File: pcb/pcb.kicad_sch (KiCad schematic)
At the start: 41 parts, among them J1 NMJ4HCD2, J2 NMJ4HCD2, J3 694106301002, SW1 FSWITCH, U1 RC4558, U2 L78L09_TO92

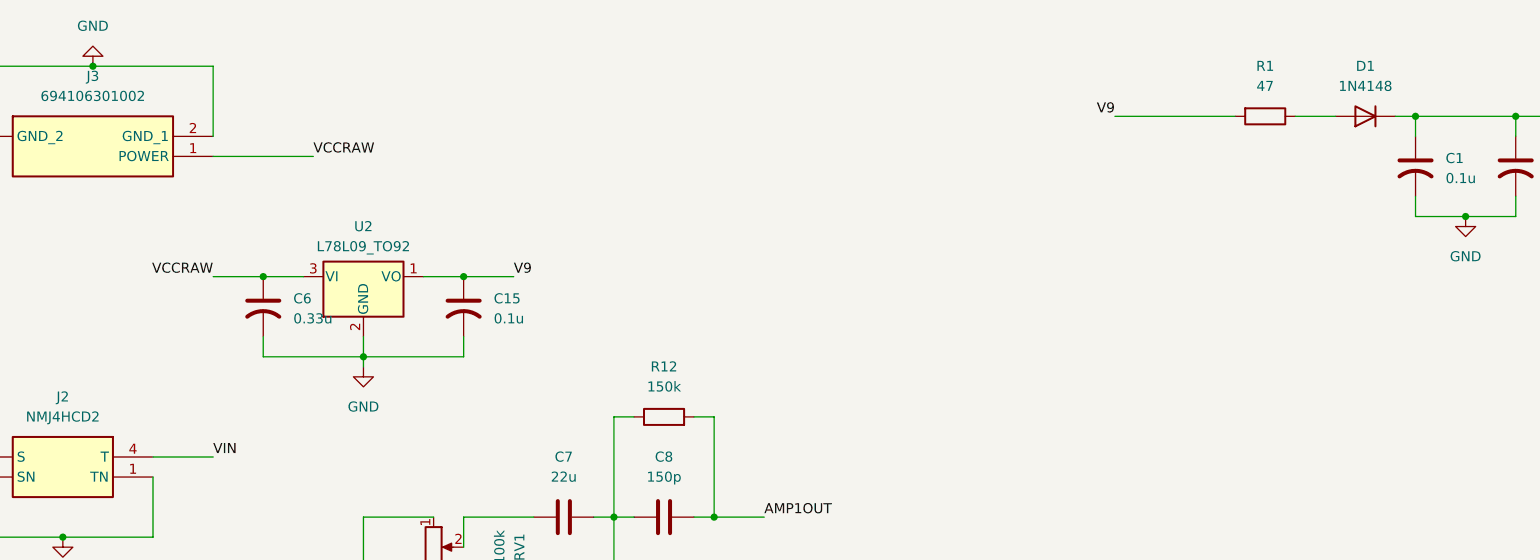
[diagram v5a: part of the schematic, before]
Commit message: Fix reverse polarity protection diode - schematic
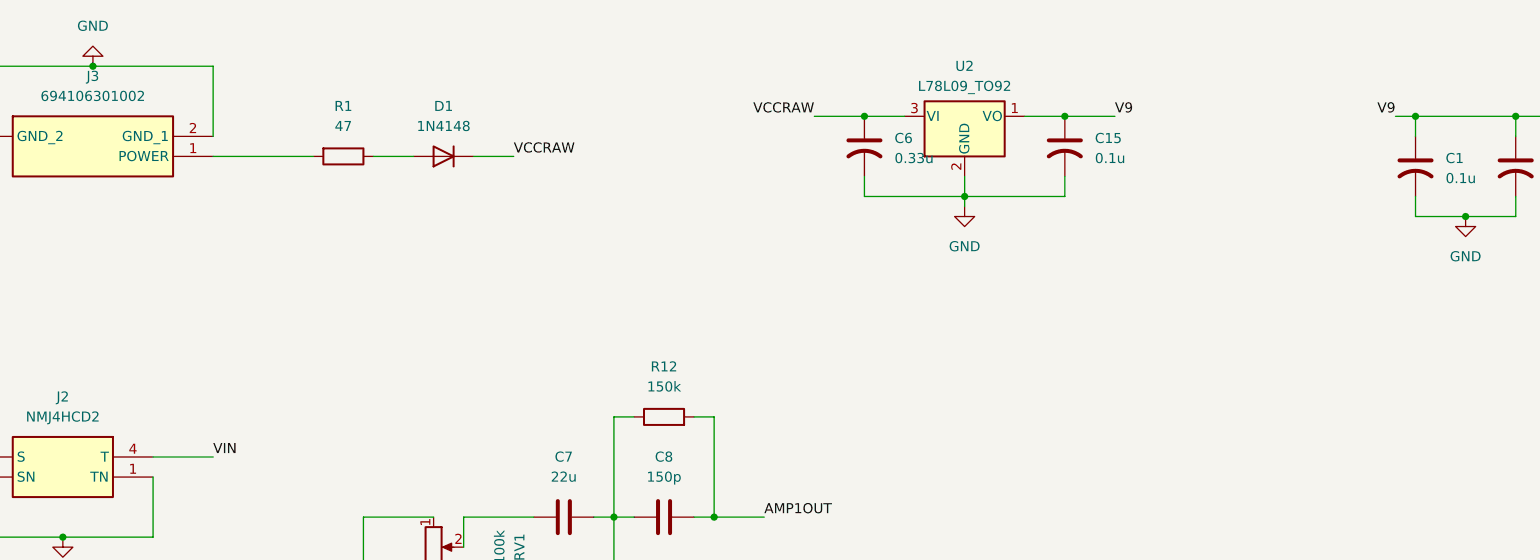
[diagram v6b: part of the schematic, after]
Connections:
- net V9: now also C1.1, C14.2, C2.1, R2.1, SW1.4, U1.8 (V+); no longer R1.2
- net VCCRAW: now also D1.1 (K); no longer J3.1 (POWER)
- removed net VCC: C1.1, C14.2, C2.1, D1.1 (K), R2.1, SW1.4, U1.8 (V+)
- new net: J3.1 (POWER), R1.2
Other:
- moved on the sheet: C15, C6, D1, R1, U2
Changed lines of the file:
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@@
 	)
 	(junction
-		(at 82.55 45.72)
+		(at 158.75 25.4)
 		(diameter 0)
 		(color 0 0 0 0)
@@
 	)
 	(junction
-		(at 69.85 55.88)
+		(at 146.05 35.56)
 		(diameter 0)
 		(color 0 0 0 0)
@@
 	)
 	(junction
-		(at 57.15 45.72)
+		(at 133.35 25.4)
 		(diameter 0)
 		(color 0 0 0 0)
@@
 	(wire
 		(pts
-			(xy 57.15 45.72) (xy 62.23 45.72)
+			(xy 133.35 25.4) (xy 138.43 25.4)
 		)
 		(stroke
@@
 	(wire
 		(pts
+			(xy 83.82 30.48) (xy 88.9 30.48)
+		)
+		(stroke
+			(width 0)
+			(type default)
+		)
+	)
+	(wire
+		(pts
 			(xy 213.36 88.9) (xy 218.44 88.9)
 		)
@@
 	(wire
 		(pts
-			(xy 69.85 53.34) (xy 69.85 55.88)
+			(xy 146.05 33.02) (xy 146.05 35.56)
 		)
 		(stroke
@@
 	(wire
 		(pts
-			(xy 187.96 25.4) (xy 193.04 25.4)
+			(xy 71.12 30.48) (xy 76.2 30.48)
 		)
 		(stroke
@@
 	(wire
 		(pts
-			(xy 50.8 45.72) (xy 57.15 45.72)
+			(xy 127 25.4) (xy 133.35 25.4)
 		)
 		(stroke
@@
 	(wire
 		(pts
-			(xy 69.85 55.88) (xy 82.55 55.88)
+			(xy 146.05 35.56) (xy 158.75 35.56)
 		)
 		(stroke
@@
 	(wire
 		(pts
-			(xy 77.47 45.72) (xy 82.55 45.72)
+			(xy 153.67 25.4) (xy 158.75 25.4)
 		)
 		(stroke
@@
 	(wire
 		(pts
-			(xy 82.55 45.72) (xy 88.9 45.72)
+			(xy 158.75 25.4) (xy 165.1 25.4)
 		)
 		(stroke
@@
 	(wire
 		(pts
-			(xy 57.15 55.88) (xy 69.85 55.88)
+			(xy 133.35 35.56) (xy 146.05 35.56)
 		)
 		(stroke
@@
 	(wire
 		(pts
-			(xy 69.85 55.88) (xy 69.85 57.15)
+			(xy 146.05 35.56) (xy 146.05 36.83)
 		)
 		(stroke
@@
 	(wire
 		(pts
-			(xy 57.15 53.34) (xy 57.15 55.88)
+			(xy 133.35 33.02) (xy 133.35 35.56)
 		)
 		(stroke
@@
 	(wire
 		(pts
-			(xy 82.55 53.34) (xy 82.55 55.88)
-		)
-		(stroke
-			(width 0)
-			(type default)
-		)
-	)
-	(wire
-		(pts
-			(xy 165.1 25.4) (xy 180.34 25.4)
+			(xy 158.75 33.02) (xy 158.75 35.56)
 		)
 		(stroke
@@
 	)
 	(label "V9"
-		(at 88.9 45.72 0)
+		(at 165.1 25.4 0)
 		(effects
 			(font
@@
 	)
 	(label "V9"
-		(at 165.1 25.4 180)
+		(at 200.66 25.4 180)
 		(effects
 			(font
@@
 	)
 	(label "VCCRAW"
-		(at 63.5 30.48 0)
+		(at 88.9 30.48 0)
 		(effects
 			(font
@@
 	)
 	(label "VCCRAW"
-		(at 50.8 45.72 180)
+		(at 127 25.4 180)
 		(effects
 			(font
@@
 	(symbol
 		(lib_id "power:GND")
-		(at 69.85 57.15 0)
+		(at 146.05 36.83 0)
 		(unit 1)
 		(exclude_from_sim no)
@@
 		(fields_autoplaced yes)
 		(property "Reference" "#PWR03"
-			(at 69.85 63.5 0)
+			(at 146.05 43.18 0)
 			(effects
 				(font
@@
 		)
 		(property "Value" "GND"
-			(at 69.85 62.23 0)
+			(at 146.05 41.91 0)
 			(effects
 				(font
@@
 		)
 		(property "Footprint" ""
-			(at 69.85 57.15 0)
+			(at 146.05 36.83 0)
 			(effects
 				(font
@@
 		)
 		(property "Datasheet" ""
-			(at 69.85 57.15 0)
+			(at 146.05 36.83 0)
 			(effects
 				(font
@@
 		)
 		(property "Description" "Power symbol creates a global label with name \"GND\" , ground"
-			(at 69.85 57.15 0)
+			(at 146.05 36.83 0)
 			(effects
 				(font
@@
 	(symbol
 		(lib_id "Device:C_US")
-		(at 82.55 49.53 0)
+		(at 158.75 29.21 0)
 		(unit 1)
 		(exclude_from_sim no)
@@
 		(fields_autoplaced yes)
 		(property "Reference" "C15"
-			(at 86.36 48.5139 0)
+			(at 162.56 28.1939 0)
 			(effects
 				(font
@@
 		)
 		(property "Value" "0.1u"
-			(at 86.36 51.0539 0)
+			(at 162.56 30.7339 0)
 			(effects
 				(font
@@
 		)
 		(property "Footprint" "Capacitor_THT:C_Radial_D5.0mm_H11.0mm_P2.00mm"
-			(at 82.55 49.53 0)
+			(at 158.75 29.21 0)
 			(effects
 				(font
@@
 		)
 		(property "Datasheet" ""
-			(at 82.55 49.53 0)
+			(at 158.75 29.21 0)
 			(effects
 				(font
@@
 		)
 		(property "Description" "capacitor, US symbol"
-			(at 82.55 49.53 0)
+			(at 158.75 29.21 0)
 			(effects
 				(font
@@
 	(symbol
 		(lib_id "Device:R")
-		(at 184.15 25.4 270)
+		(at 67.31 30.48 270)
 		(unit 1)
 		(exclude_from_sim no)
@@
 		(fields_autoplaced yes)
 		(property "Reference" "R1"
-			(at 184.15 19.05 90)
+			(at 67.31 24.13 90)
 			(effects
 				(font
@@
 		)
 		(property "Value" "47"
-			(at 184.15 21.59 90)
+			(at 67.31 26.67 90)
 			(effects
 				(font
@@
 		)
 		(property "Footprint" "Resistor_THT:R_Axial_DIN0207_L6.3mm_D2.5mm_P10.16mm_Horizontal"
-			(at 184.15 23.622 90)
+			(at 67.31 28.702 90)
 			(effects
 				(font
@@
 		)
 		(property "Datasheet" "~"
-			(at 184.15 25.4 0)
+			(at 67.31 30.48 0)
 			(effects
 				(font
@@
 		)
 		(property "Description" "Resistor"
-			(at 184.15 25.4 0)
+			(at 67.31 30.48 0)
 			(effects
 				(font
@@
 	(symbol
 		(lib_id "Regulator_Linear:L78L09_TO92")
-		(at 69.85 45.72 0)
+		(at 146.05 25.4 0)
 		(unit 1)
 		(exclude_from_sim no)
@@
 		(fields_autoplaced yes)
 		(property "Reference" "U2"
-			(at 69.85 39.37 0)
+			(at 146.05 19.05 0)
 			(effects
 				(font
@@
 		)
 		(property "Value" "L78L09_TO92"
-			(at 69.85 41.91 0)
+			(at 146.05 21.59 0)
 			(effects
 				(font
@@
 		)
 		(property "Footprint" "Package_TO_SOT_THT:TO-92_Inline"
-			(at 69.85 40.005 0)
+			(at 146.05 19.685 0)
 			(effects
 				(font
@@
 		)
 		(property "Datasheet" "http://www.st.com/content/ccc/resource/technical/document/datasheet/15/55/e5/aa/23/5b/43/fd/CD00000446.pdf/files/CD00000446.pdf/jcr:content/translations/en.CD00000446.pdf"
-			(at 69.85 46.99 0)
+			(at 146.05 26.67 0)
 			(effects
 				(font
@@
 		)
 		(property "Description" "Positive 100mA 30V Linear Regulator, Fixed Output 9V, TO-92"
-			(at 69.85 45.72 0)
+			(at 146.05 25.4 0)
 			(effects
 				(font
@@
 	(symbol
 		(lib_id "Diode:1N4148")
-		(at 196.85 25.4 180)
+		(at 80.01 30.48 180)
 		(unit 1)
 		(exclude_from_sim no)
@@
 		(fields_autoplaced yes)
 		(property "Reference" "D1"
-			(at 196.85 19.05 0)
+			(at 80.01 24.13 0)
 			(effects
 				(font
@@
 		)
 		(property "Value" "1N4148"
-			(at 196.85 21.59 0)
+			(at 80.01 26.67 0)
 			(effects
 				(font
@@
 		)
 		(property "Footprint" "Diode_THT:D_DO-35_SOD27_P7.62mm_Horizontal"
-			(at 196.85 25.4 0)
+			(at 80.01 30.48 0)
 			(effects
 				(font
@@
 		)
 		(property "Datasheet" "https://assets.nexperia.com/documents/data-sheet/1N4148_1N4448.pdf"
-			(at 196.85 25.4 0)
+			(at 80.01 30.48 0)
 			(effects
 				(font
@@
 		)
 		(property "Description" "100V 0.15A standard switching diode, DO-35"
-			(at 196.85 25.4 0)
+			(at 80.01 30.48 0)
 			(effects
 				(font
@@
 		)
 		(property "Sim.Device" "D"
-			(at 196.85 25.4 0)
+			(at 80.01 30.48 0)
 			(effects
 				(font
@@
 		)
 		(property "Sim.Pins" "1=K 2=A"
-			(at 196.85 25.4 0)
+			(at 80.01 30.48 0)
 			(effects
 				(font
@@
 	(symbol
 		(lib_id "Device:C_US")
-		(at 57.15 49.53 0)
+		(at 133.35 29.21 0)
 		(unit 1)
 		(exclude_from_sim no)
@@
 		(fields_autoplaced yes)
 		(property "Reference" "C6"
-			(at 60.96 48.5139 0)
+			(at 137.16 28.1939 0)
 			(effects
 				(font
@@
 		)
 		(property "Value" "0.33u"
-			(at 60.96 51.0539 0)
+			(at 137.16 30.7339 0)
 			(effects
 				(font
@@
 		)
 		(property "Footprint" "Capacitor_THT:C_Radial_D5.0mm_H11.0mm_P2.00mm"
-			(at 57.15 49.53 0)
+			(at 133.35 29.21 0)
 			(effects
 				(font
@@
 		)
 		(property "Datasheet" ""
-			(at 57.15 49.53 0)
+			(at 133.35 29.21 0)
 			(effects
 				(font
@@
 		)
 		(property "Description" "capacitor, US symbol"
-			(at 57.15 49.53 0)
+			(at 133.35 29.21 0)
 			(effects
 				(font
